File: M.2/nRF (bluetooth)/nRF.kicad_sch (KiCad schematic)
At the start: 3 parts

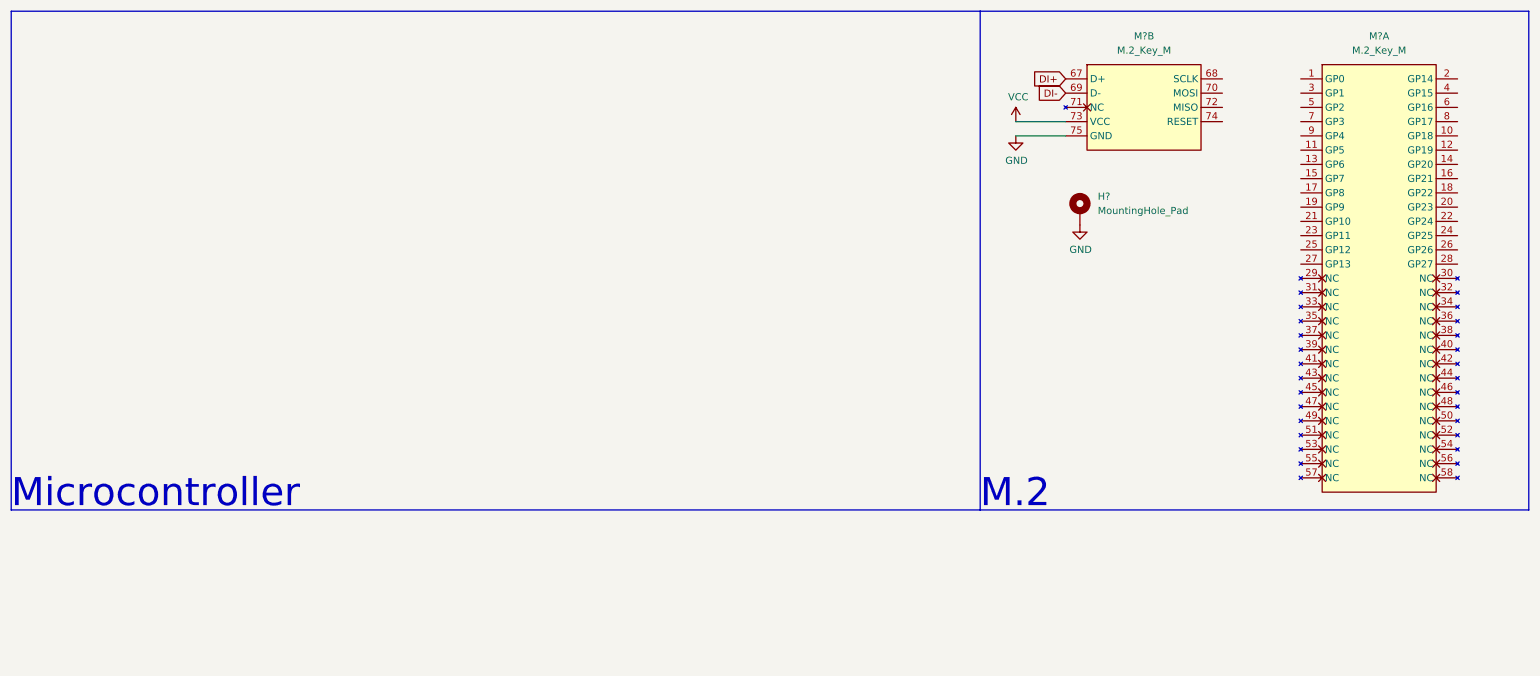
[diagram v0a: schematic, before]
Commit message: Add the files for different M.2 Boards and work on STM32F411
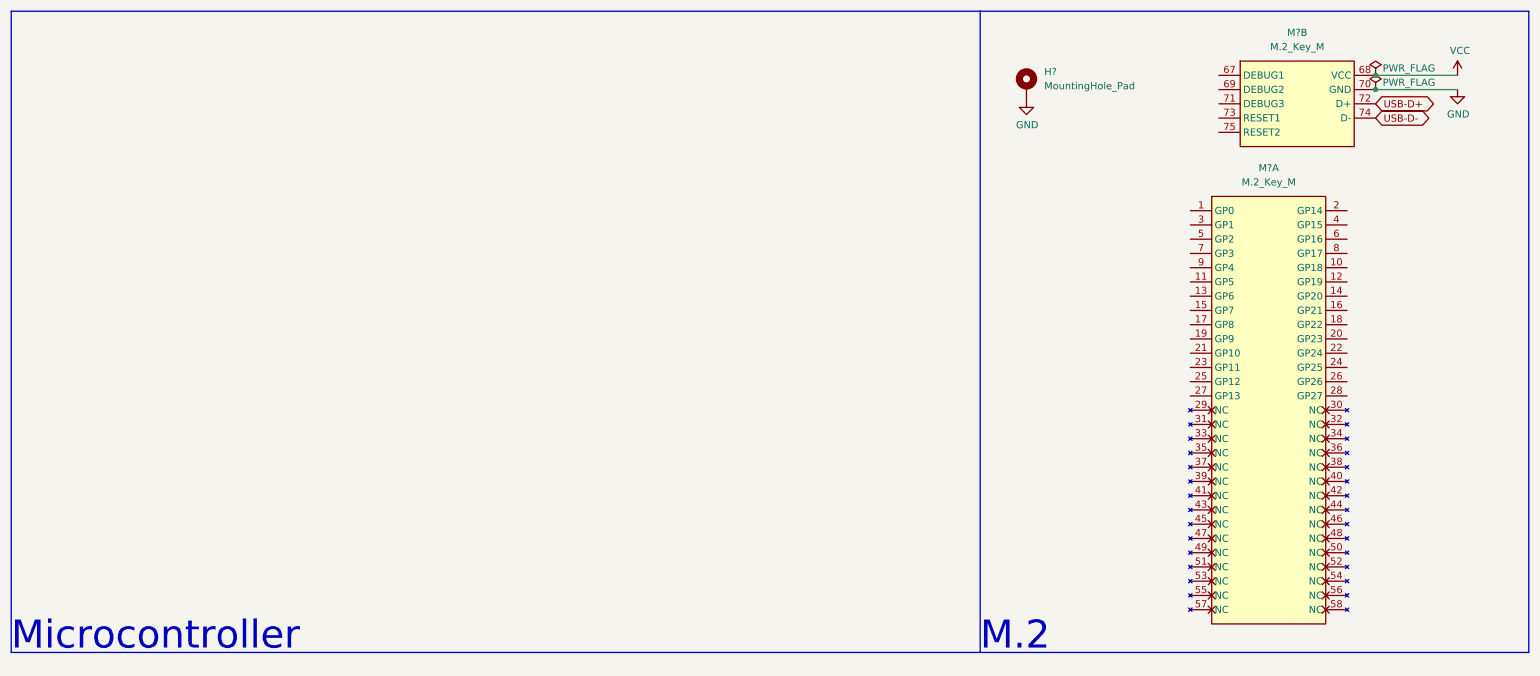
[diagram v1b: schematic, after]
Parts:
- removed H?: MountingHole_Pad, MountingHole:MountingHole_2.2mm_M2_ISO7380_Pad, symbol Mechanical:MountingHole_Pad
- removed M? (x2): M.2_Key_M, m2ngff:m2-padKeyM, symbol m2ngff:M.2_Key_M
- added H?: MountingHole_Pad, MountingHole:MountingHole_2.2mm_M2_ISO7380_Pad, symbol Mechanical:MountingHole_Pad
- added M? (x2): M.2_Key_M, m2ngff:m2-padKeyM, symbol m2ngff:M.2_Key_M
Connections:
- net GND: now also H?.1, M?.70 (GND)
- net VCC: now also M?.68 (VCC)
- new net USB-D+: M?.72 (D+)
- new net USB-D-: M?.74 (D-)

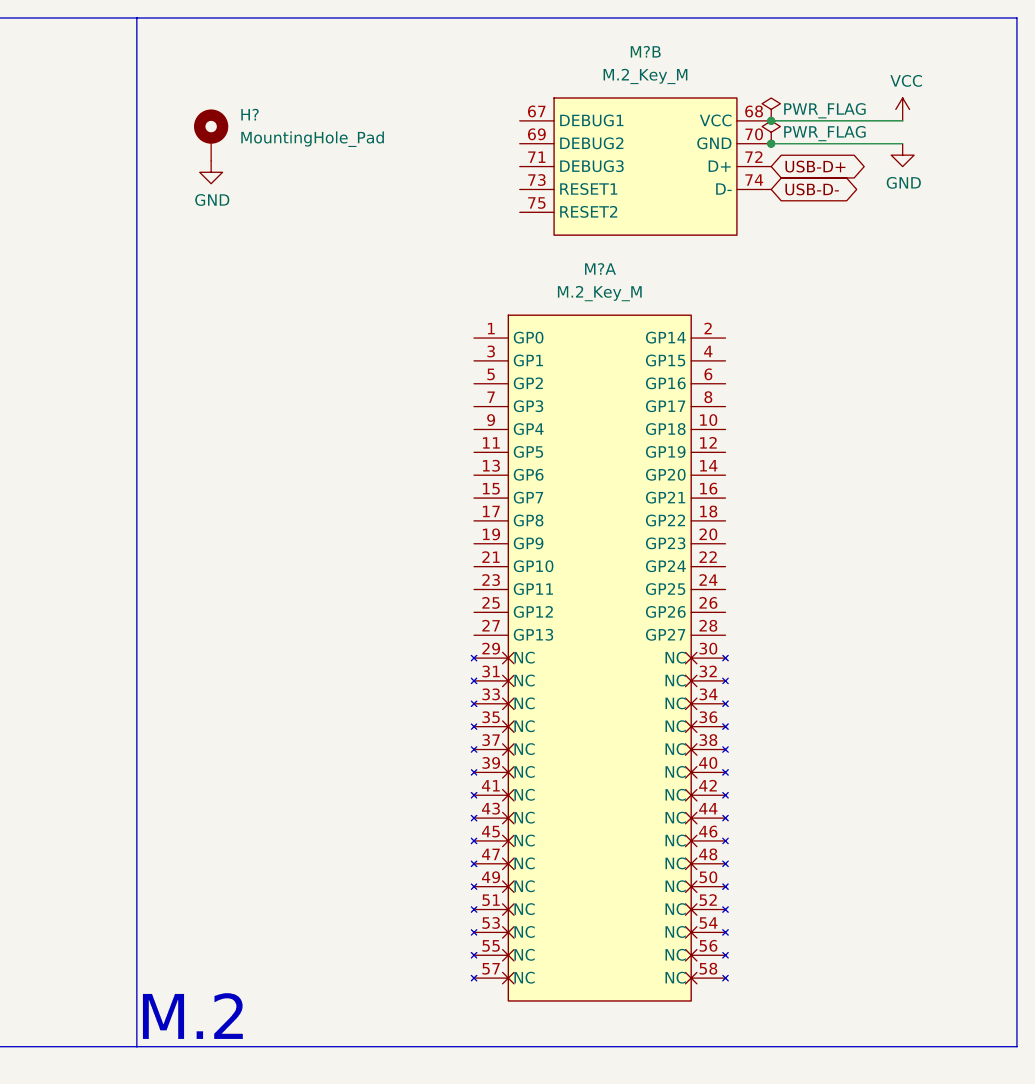
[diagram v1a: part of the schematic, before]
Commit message: change the rest to key e, change the template
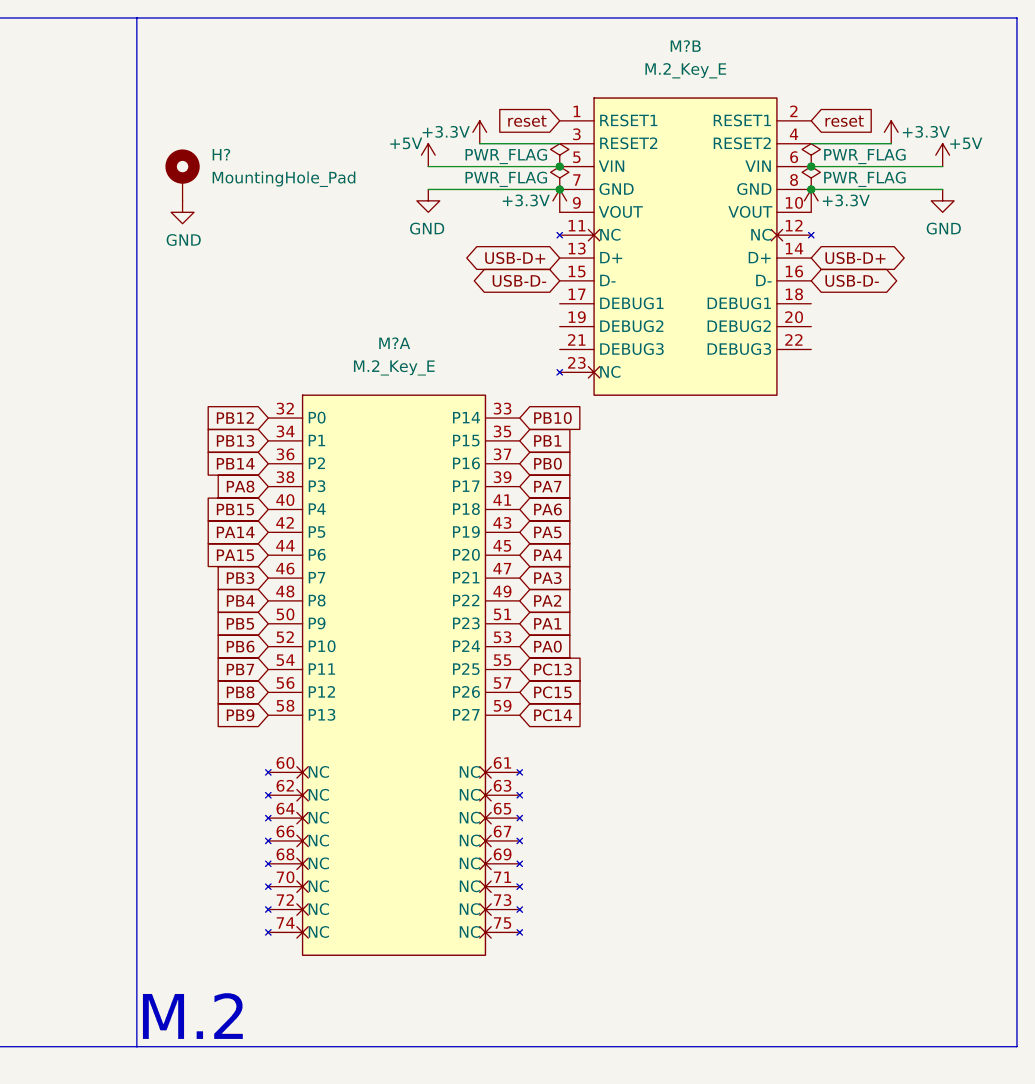
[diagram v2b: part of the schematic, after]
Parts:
- removed H?: MountingHole_Pad, MountingHole:MountingHole_2.2mm_M2_ISO7380_Pad, symbol Mechanical:MountingHole_Pad
- removed M? (x2): M.2_Key_M, m2ngff:m2-padKeyM, symbol m2ngff:M.2_Key_M
- added H?: MountingHole_Pad, MountingHole:MountingHole_2.2mm_M2_ISO7380_Pad, symbol Mechanical:MountingHole_Pad
- added M? (x2): M.2_Key_E, m2ngff:m2-padKeyE, symbol m2ngff:M.2_Key_E
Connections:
- net GND: now also H?.1, M?.7 (GND), M?.8 (GND)
- net USB-D+: now also M?.13 (D+), M?.14 (D+)
- net USB-D-: now also M?.15 (D-), M?.16 (D-)
- new net +3V3: M?.10 (VOUT), M?.3 (RESET2), M?.4 (RESET2), M?.9 (VOUT)
- new net +5V: M?.5 (VIN), M?.6 (VIN)
- new net PA0: M?.53 (P24)
- new net PA1: M?.51 (P23)
- new net PA14: M?.42 (P5)
- new net PA15: M?.44 (P6)
- new net PA2: M?.49 (P22)
- new net PA3: M?.47 (P21)
- new net PA4: M?.45 (P20)
- new net PA5: M?.43 (P19)
- new net PA6: M?.41 (P18)
- new net PA7: M?.39 (P17)
- new net PA8: M?.38 (P3)
- new net PB0: M?.37 (P16)
- new net PB1: M?.35 (P15)
- new net PB10: M?.33 (P14)
- new net PB12: M?.32 (P0)
- new net PB13: M?.34 (P1)
- new net PB14: M?.36 (P2)
- new net PB15: M?.40 (P4)
- new net PB3: M?.46 (P7)
- new net PB4: M?.48 (P8)
- new net PB5: M?.50 (P9)
- new net PB6: M?.52 (P10)
- new net PB7: M?.54 (P11)
- new net PB8: M?.56 (P12)
- new net PB9: M?.58 (P13)
- new net PC13: M?.55 (P25)
- new net PC14: M?.59 (P27)
- new net PC15: M?.57 (P26)
- new net reset: M?.1 (RESET1), M?.2 (RESET1)

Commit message: finish working on stmf411
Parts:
- removed H?: MountingHole_Pad, MountingHole:MountingHole_2.2mm_M2_ISO7380_Pad, symbol Mechanical:MountingHole_Pad
- added H?: MountingHole_Pad, MountingHole:MountingHole_2.2mm_M2_Pad_Via, symbol Mechanical:MountingHole_Pad
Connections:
- net GND: now also H?.1
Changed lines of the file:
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@@
-    (pin "1")
-  )
-  (symbol (lib_id "Mechanical:MountingHole_Pad") (at 191.135 31.115 0) (unit 1)
-    (in_bom yes) (on_board yes) (fields_autoplaced)
-    (property "Reference" "H?" (id 0) (at 194.31 28.5749 0)
-      (effects (font (size 1.27 1.27)) (justify left))
-    )
-    (property "Value" "MountingHole_Pad" (id 1) (at 194.31 31.1149 0)
-      (effects (font (size 1.27 1.27)) (justify left))
-    )
-    (property "Footprint" "MountingHole:MountingHole_2.2mm_M2_ISO7380_Pad" (id 2) (at 191.135 31.115 0)
-      (effects (font (size 1.27 1.27)) hide)
-    )
-    (property "Datasheet" "~" (id 3) (at 191.135 31.115 0)
-      (effects (font (size 1.27 1.27)) hide)
-    )
     (pin "1")
   )
@@
     (pin "9")
   )
+  (symbol (lib_id "Power:GND") (at 192.405 26.67 0) (unit 1)
+    (in_bom yes) (on_board yes)
+    (property "Reference" "#PWR?" (id 0) (at 192.405 33.02 0)
+      (effects (font (size 1.27 1.27)) hide)
+    )
+    (property "Value" "GND" (id 1) (at 192.532 31.0642 0))
+    (property "Footprint" "" (id 2) (at 192.405 26.67 0)
+      (effects (font (size 1.27 1.27)) hide)
+    )
+    (property "Datasheet" "" (id 3) (at 192.405 26.67 0)
+      (effects (font (size 1.27 1.27)) hide)
+    )
+    (pin "1")
+  )
   (symbol (lib_id "Power:GND") (at 275.59 32.385 0) (unit 1)
     (in_bom yes) (on_board yes)
@@
     )
     (property "Datasheet" "" (id 3) (at 224.155 27.305 0)
-      (effects (font (size 1.27 1.27)) hide)
-    )
-    (pin "1")
-  )
-  (symbol (lib_id "Power:GND") (at 191.135 33.655 0) (unit 1)
-    (in_bom yes) (on_board yes)
-    (property "Reference" "#PWR?" (id 0) (at 191.135 40.005 0)
-      (effects (font (size 1.27 1.27)) hide)
-    )
-    (property "Value" "GND" (id 1) (at 191.262 38.0492 0))
-    (property "Footprint" "" (id 2) (at 191.135 33.655 0)
-      (effects (font (size 1.27 1.27)) hide)
-    )
-    (property "Datasheet" "" (id 3) (at 191.135 33.655 0)
       (effects (font (size 1.27 1.27)) hide)
     )
@@
     (pin "75")
   )
+  (symbol (lib_id "Mechanical:MountingHole_Pad") (at 192.405 24.13 0) (unit 1)
+    (in_bom yes) (on_board yes) (fields_autoplaced)
+    (property "Reference" "H?" (id 0) (at 195.58 21.5899 0)
+      (effects (font (size 1.27 1.27)) (justify left))
+    )
+    (property "Value" "MountingHole_Pad" (id 1) (at 195.58 24.1299 0)
+      (effects (font (size 1.27 1.27)) (justify left))
+    )
+    (property "Footprint" "MountingHole:MountingHole_2.2mm_M2_Pad_Via" (id 2) (at 192.405 24.13 0)
+      (effects (font (size 1.27 1.27)) hide)
+    )
+    (property "Datasheet" "~" (id 3) (at 192.405 24.13 0)
+      (effects (font (size 1.27 1.27)) hide)
+    )
+    (pin "1")
+  )
   (symbol (lib_id "power:PWR_FLAG") (at 260.985 32.385 0) (unit 1)
     (in_bom yes) (on_board yes)
@@
       (reference "#PWR?") (unit 1) (value "GND") (footprint "")
     )
+    (path "/b4afdd30-7a78-4cd8-8670-bb6dd787dcdc"
+      (reference "#PWR?") (unit 1) (value "GND") (footprint "")
+    )
     (path "/b9f8ba78-9b7b-4a7c-8351-c9f145a140ab"
       (reference "#PWR?") (unit 1) (value "GND") (footprint "")
@@
       (reference "#PWR?") (unit 1) (value "+3.3V") (footprint "")
     )
-    (path "/e61e3b10-16bb-45fa-9a42-277efd2ec104"
-      (reference "#PWR?") (unit 1) (value "GND") (footprint "")
-    )
     (path "/e9febdd1-669e-46f3-983e-2ded7b5fa339"
       (reference "#PWR?") (unit 1) (value "+5V") (footprint "")
     )
-    (path "/8f0c1305-7bd7-41b0-a77d-0a9232a17e2e"
-      (reference "H?") (unit 1) (value "MountingHole_Pad") (footprint "MountingHole:MountingHole_2.2mm_M2_ISO7380_Pad")
+    (path "/f61adca3-c1e4-457e-8212-9dc978cabab5"
+      (reference "H?") (unit 1) (value "MountingHole_Pad") (footprint "MountingHole:MountingHole_2.2mm_M2_Pad_Via")
     )
     (path "/eb79b938-dc23-4503-beb0-3634b653c9e4"
